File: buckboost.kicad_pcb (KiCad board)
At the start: 2 copper layers, 48.9 x 26 mm, 27 parts, among them K1 CONN_3, P1 CONN_2, P2 CONN_2, SW1 SPST, U1 TPS63060

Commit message: Revision 1
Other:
- board text added: "Revision 1"
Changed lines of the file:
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@@
     (area 64.694999 132.004999 113.740001 158.190001)
     (thickness 1.6)
-    (drawings 21)
+    (drawings 22)
     (tracks 104)
     (zones 0)
@@
     )
   )
+  (gr_text "Revision 1" (at 71.755 156.21) (layer B.SilkS)
+    (effects (font (size 1.5 1.5) (thickness 0.3)) (justify mirror))
+  )
   (gr_text "TPS63060 Power Supply\nby Amperture Engineering" (at 97.155 154.305) (layer B.SilkS)

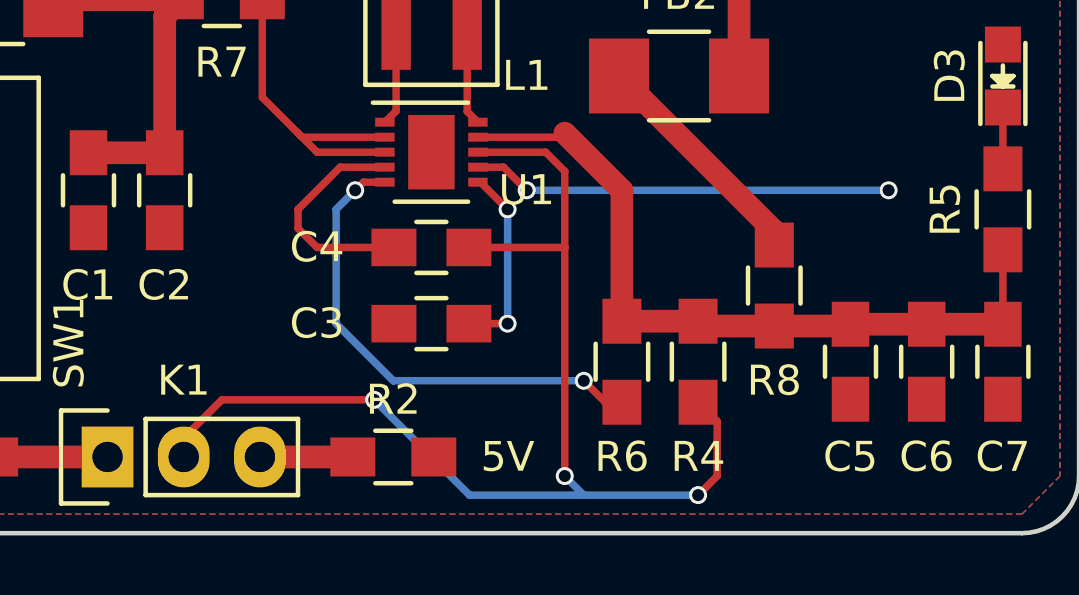
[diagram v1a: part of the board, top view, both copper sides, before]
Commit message: Fixing tracks for OSHPark design rules.
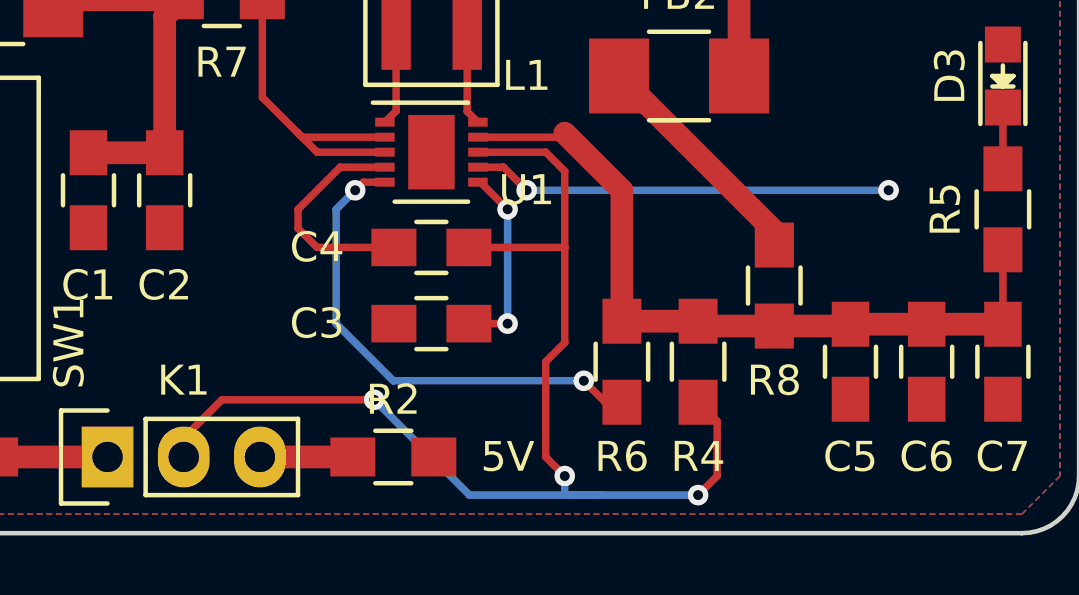
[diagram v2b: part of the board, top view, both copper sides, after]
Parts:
- gave numbers to parts that had none: 1
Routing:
- net FEEDBACK: track 40.7 -> 42.8 mm
- net PG: track 17.1 -> 17.6 mm
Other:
- net class Default: clearance 0.2 -> 0.1524; via_dia 0.6 -> 0.6858; via_drill 0.4 -> 0.3302
- rule trace_clearance: 0.2 -> 0.1524
- rule trace_min: 0.2 -> 0.1524
- rule via_min_drill: 0.3 -> 0.3302
- rule via_min_size: 0.4 -> 0.6858
- board text removed: "Revision 1"
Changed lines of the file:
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@@
     (area 64.694999 132.004999 113.740001 158.190001)
     (thickness 1.6)
-    (drawings 22)
-    (tracks 104)
+    (drawings 21)
+    (tracks 110)
     (zones 0)
     (modules 27)
@@
   (setup
     (last_trace_width 0.25)
-    (trace_clearance 0.2)
+    (trace_clearance 0.1524)
     (zone_clearance 0.508)
-    (zone_45_only no)
-    (trace_min 0.2)
+    (zone_45_only yes)
+    (trace_min 0.1524)
     (segment_width 0.2)
     (edge_width 0.15)
-    (via_size 0.6)
-    (via_drill 0.4)
-    (via_min_size 0.4)
-    (via_min_drill 0.3)
-    (uvia_size 0.3)
-    (uvia_drill 0.1)
+    (via_size 0.6858)
+    (via_drill 0.3302)
+    (via_min_size 0.6858)
+    (via_min_drill 0.3302)
+    (uvia_size 0.762)
+    (uvia_drill 0.508)
     (uvias_allowed no)
     (uvia_min_size 0)
@@
   (net 18 VOUT)
   (net_class Default "This is the default net class."
-    (clearance 0.2)
+    (clearance 0.1524)
     (trace_width 0.25)
-    (via_dia 0.6)
-    (via_drill 0.4)
-    (uvia_dia 0.3)
-    (uvia_drill 0.1)
+    (via_dia 0.6858)
+    (via_drill 0.3302)
+    (uvia_dia 0.762)
+    (uvia_drill 0.508)
     (add_net FEEDBACK)
     (add_net GND)
@@
     (descr "Symbol, OSHW-Logo, Silk Screen,")
     (tags "Symbol, OSHW-Logo, Silk Screen,")
-    (fp_text reference "" (at 0.09906 4.38912 180) (layer B.SilkS) hide
+    (fp_text reference REF** (at 0.09906 4.38912 180) (layer B.SilkS) hide
       (effects (font (size 1 1) (thickness 0.15)) (justify mirror))
     )
@@
     )
   )
-  (gr_text "Revision 1" (at 71.755 156.21) (layer B.SilkS)
-    (effects (font (size 1.5 1.5) (thickness 0.3)) (justify mirror))
-  )
   (gr_text "TPS63060 Power Supply\nby Amperture Engineering" (at 97.155 154.305) (layer B.SilkS)
     (effects (font (size 1.5 1.5) (thickness 0.3)) (justify mirror))
@@
   (segment (start 79.47 140.335) (end 83.9 135.905) (width 0.25) (layer F.Cu) (net 1))
   (segment (start 83.9 135.905) (end 83.9 135.255) (width 0.25) (layer F.Cu) (net 1))
+  (segment (start 93.625 145.915) (end 94.48 145.915) (width 0.25) (layer F.Cu) (net 2))
+  (via (at 107.315 146.685) (size 0.6858) (drill 0.3302) (layers F.Cu B.Cu) (net 2))
+  (segment (start 95.25 146.685) (end 107.315 146.685) (width 0.25) (layer B.Cu) (net 2))
+  (via (at 95.25 146.685) (size 0.6858) (drill 0.3302) (layers F.Cu B.Cu) (net 2))
+  (segment (start 94.48 145.915) (end 95.25 146.685) (width 0.25) (layer F.Cu) (net 2))
   (segment (start 90.525 145.915) (end 89.035 145.915) (width 0.25) (layer F.Cu) (net 2))
   (segment (start 88.265 148.59) (end 90.825 148.59) (width 0.25) (layer F.Cu) (net 2))
@@
   (segment (start 87.63 147.32) (end 87.63 147.955) (width 0.25) (layer F.Cu) (net 2))
   (segment (start 89.035 145.915) (end 87.63 147.32) (width 0.25) (layer F.Cu) (net 2))
-  (segment (start 93.625 145.915) (end 94.48 145.915) (width 0.25) (layer F.Cu) (net 2))
-  (via (at 107.315 146.685) (size 0.6) (drill 0.4) (layers F.Cu B.Cu) (net 2))
-  (segment (start 95.25 146.685) (end 107.315 146.685) (width 0.25) (layer B.Cu) (net 2))
-  (via (at 95.25 146.685) (size 0.6) (drill 0.4) (layers F.Cu B.Cu) (net 2))
-  (segment (start 94.48 145.915) (end 95.25 146.685) (width 0.25) (layer F.Cu) (net 2))
   (segment (start 93.625 146.415) (end 93.71 146.415) (width 0.25) (layer F.Cu) (net 3))
   (segment (start 93.71 146.415) (end 94.615 147.32) (width 0.25) (layer F.Cu) (net 3))
-  (via (at 94.615 147.32) (size 0.6) (drill 0.4) (layers F.Cu B.Cu) (net 3))
+  (segment (start 94.615 151.13) (end 93.325 151.13) (width 0.25) (layer F.Cu) (net 3))
+  (via (at 94.615 151.13) (size 0.6858) (drill 0.3302) (layers F.Cu B.Cu) (net 3))
   (segment (start 94.615 147.32) (end 94.615 151.13) (width 0.25) (layer B.Cu) (net 3))
-  (via (at 94.615 151.13) (size 0.6) (drill 0.4) (layers F.Cu B.Cu) (net 3))
-  (segment (start 94.615 151.13) (end 93.325 151.13) (width 0.25) (layer F.Cu) (net 3))
+  (via (at 94.615 147.32) (size 0.6858) (drill 0.3302) (layers F.Cu B.Cu) (net 3))
+  (segment (start 96.52 148.59) (end 96.52 151.765) (width 0.25) (layer F.Cu) (net 4))
+  (segment (start 96.52 156.845) (end 97.79 156.845) (width 0.25) (layer B.Cu) (net 4))
+  (segment (start 96.52 156.21) (end 96.52 156.845) (width 0.25) (layer B.Cu) (net 4))
+  (via (at 96.52 156.21) (size 0.6858) (drill 0.3302) (layers F.Cu B.Cu) (net 4))
+  (segment (start 95.885 155.575) (end 96.52 156.21) (width 0.25) (layer F.Cu) (net 4))
+  (segment (start 95.885 152.4) (end 95.885 155.575) (width 0.25) (layer F.Cu) (net 4))
+  (segment (start 96.52 151.765) (end 95.885 152.4) (width 0.25) (layer F.Cu) (net 4))
+  (segment (start 100.965 153.75) (end 101.6 154.385) (width 0.25) (layer F.Cu) (net 4))
+  (segment (start 101.6 154.385) (end 101.6 156.21) (width 0.25) (layer F.Cu) (net 4))
+  (segment (start 101.6 156.21) (end 100.965 156.845) (width 0.25) (layer F.Cu) (net 4))
+  (via (at 100.965 156.845) (size 0.6858) (drill 0.3302) (layers F.Cu B.Cu) (net 4))
+  (segment (start 100.965 156.845) (end 97.79 156.845) (width 0.25) (layer B.Cu) (net 4))
+  (segment (start 85.09 153.67) (end 83.82 154.94) (width 0.25) (layer F.Cu) (net 4))
+  (segment (start 97.79 156.845) (end 93.345 156.845) (width 0.25) (layer B.Cu) (net 4))
+  (segment (start 93.345 156.845) (end 90.17 153.67) (width 0.25) (layer B.Cu) (net 4))
+  (via (at 90.17 153.67) (size 0.6858) (drill 0.3302) (layers F.Cu B.Cu) (net 4))
+  (segment (start 90.17 153.67) (end 85.09 153.67) (width 0.25) (layer F.Cu) (net 4))
+  (segment (start 83.82 154.94) (end 83.82 155.575) (width 0.25) (layer F.Cu) (net 4))
   (segment (start 93.325 148.59) (end 96.52 148.59) (width 0.25) (layer F.Cu) (net 4))
   (segment (start 83.82 155.575) (end 83.82 154.94) (width 0.25) (layer F.Cu) (net 4))
-  (segment (start 83.82 154.94) (end 85.09 153.67) (width 0.25) (layer F.Cu) (net 4))
-  (segment (start 85.09 153.67) (end 90.17 153.67) (width 0.25) (layer F.Cu) (net 4))
-  (via (at 90.17 153.67) (size 0.6) (drill 0.4) (layers F.Cu B.Cu) (net 4))
-  (segment (start 90.17 153.67) (end 93.345 156.845) (width 0.25) (layer B.Cu) (net 4))
-  (segment (start 93.345 156.845) (end 97.155 156.845) (width 0.25) (layer B.Cu) (net 4))
   (segment (start 93.625 145.415) (end 95.885 145.415) (width 0.25) (layer F.Cu) (net 4))
-  (segment (start 101.6 156.21) (end 101.6 154.385) (width 0.25) (layer F.Cu) (net 4))
-  (segment (start 100.965 156.845) (end 101.6 156.21) (width 0.25) (layer F.Cu) (net 4))
-  (via (at 100.965 156.845) (size 0.6) (drill 0.4) (layers F.Cu B.Cu) (net 4))
-  (segment (start 97.155 156.845) (end 100.965 156.845) (width 0.25) (layer B.Cu) (net 4))
-  (segment (start 96.52 156.21) (end 97.155 156.845) (width 0.25) (layer B.Cu) (net 4))
-  (via (at 96.52 156.21) (size 0.6) (drill 0.4) (layers F.Cu B.Cu) (net 4))
   (segment (start 96.52 146.05) (end 96.52 148.59) (width 0.25) (layer F.Cu) (net 4))
-  (segment (start 96.52 148.59) (end 96.52 156.21) (width 0.25) (layer F.Cu) (net 4))
   (segment (start 95.885 145.415) (end 96.52 146.05) (width 0.25) (layer F.Cu) (net 4))
-  (segment (start 101.6 154.385) (end 100.965 153.75) (width 0.25) (layer F.Cu) (net 4))
   (segment (start 98.425 151.05) (end 98.425 146.685) (width 0.758) (layer F.Cu) (net 5))
   (segment (start 98.425 146.685) (end 96.52 144.78) (width 0.758) (layer F.Cu) (net 5))
@@
   (segment (start 90.525 146.415) (end 89.805 146.415) (width 0.25) (layer F.Cu) (net 12))
   (segment (start 97.155 153.035) (end 97.87 153.75) (width 0.25) (layer F.Cu) (net 12))
-  (via (at 97.155 153.035) (size 0.6) (drill 0.4) (layers F.Cu B.Cu) (net 12))
+  (via (at 97.155 153.035) (size 0.6858) (drill 0.3302) (layers F.Cu B.Cu) (net 12))
   (segment (start 90.805 153.035) (end 97.155 153.035) (width 0.25) (layer B.Cu) (net 12))
   (segment (start 88.9 151.13) (end 90.805 153.035) (width 0.25) (layer B.Cu) (net 12))
   (segment (start 88.9 147.32) (end 88.9 151.13) (width 0.25) (layer B.Cu) (net 12))
   (segment (start 89.535 146.685) (end 88.9 147.32) (width 0.25) (layer B.Cu) (net 12))
-  (via (at 89.535 146.685) (size 0.6) (drill 0.4) (layers F.Cu B.Cu) (net 12))
+  (via (at 89.535 146.685) (size 0.6858) (drill 0.3302) (layers F.Cu B.Cu) (net 12))
   (segment (start 89.805 146.415) (end 89.535 146.685) (width 0.25) (layer F.Cu) (net 12))
   (segment (start 97.87 153.75) (end 98.425 153.75) (width 0.25) (layer F.Cu) (net 12))
+  (segment (start 97.87 153.75) (end 98.425 153.75) (width 0.25) (layer F.Cu) (net 12))
   (segment (start 98.425 153.75) (end 98.425 154.305) (width 0.25) (layer F.Cu) (net 12))

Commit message: Housecleaning
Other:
- board text added: "Rev1"
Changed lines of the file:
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@@
     (area 64.694999 132.004999 113.740001 158.190001)
     (thickness 1.6)
-    (drawings 21)
+    (drawings 22)
     (tracks 110)
     (zones 0)
@@
   (page A4)
   (layers
-    (0 F.Cu signal)
-    (31 B.Cu signal)
-    (32 B.Adhes user)
-    (33 F.Adhes user)
-    (34 B.Paste user)
-    (35 F.Paste user)
+    (0 F.Cu signal hide)
+    (31 B.Cu signal hide)
+    (32 B.Adhes user hide)
+    (33 F.Adhes user hide)
+    (34 B.Paste user hide)
+    (35 F.Paste user hide)
     (36 B.SilkS user)
     (37 F.SilkS user)
-    (38 B.Mask user)
-    (39 F.Mask user)
-    (40 Dwgs.User user)
-    (41 Cmts.User user)
+    (38 B.Mask user hide)
+    (39 F.Mask user hide)
+    (40 Dwgs.User user hide)
+    (41 Cmts.User user hide)
     (42 Eco1.User user hide)
-    (43 Eco2.User user)
+    (43 Eco2.User user hide)
     (44 Edge.Cuts user)
     (45 Margin user)
@@
     (pad_to_mask_clearance 0.2)
     (aux_axis_origin 0 0)
-    (visible_elements FFFEFF7F)
+    (visible_elements FFFF3FFF)
     (pcbplotparams
-      (layerselection 0x00030_80000001)
-      (usegerberextensions false)
+      (layerselection 0x010f0_80000001)
+      (usegerberextensions true)
       (excludeedgelayer true)
       (linewidth 0.100000)
@@
       (outputformat 1)
       (mirror false)
-      (drillshape 1)
+      (drillshape 0)
       (scaleselection 1)
-      (outputdirectory ""))
+      (outputdirectory gerb/))
   )
   (net 0 "")
@@
     )
   )
-  (gr_text "TPS63060 Power Supply\nby Amperture Engineering" (at 97.155 154.305) (layer B.SilkS)
+  (gr_text Rev1 (at 109.855 155.575) (layer B.SilkS)
     (effects (font (size 1.5 1.5) (thickness 0.3)) (justify mirror))
   )
+  (gr_text "TPS63060 Power Supply\nby Amperture Engineering" (at 98.425 149.86) (layer B.SilkS)
+    (effects (font (size 1.5 1.5) (thickness 0.3)) (justify mirror))
+  )

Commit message: Preview of schematic
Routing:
- net Net-(C1-Pad1): track 28.4 -> 35.3 mm
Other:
- net class thick added: clearance 0.1524, trace_width 0.758, via_dia 0.6858, via_drill 0.3302
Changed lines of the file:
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@@
     (links 43)
     (no_connects 0)
-    (area 64.694999 132.004999 113.740001 158.190001)
+    (area 83.703572 83.43348 172.2224 156.775)
     (thickness 1.6)
     (drawings 22)
-    (tracks 110)
+    (tracks 112)
     (zones 0)
     (modules 27)
@@
   (page A4)
   (layers
-    (0 F.Cu signal hide)
-    (31 B.Cu signal hide)
-    (32 B.Adhes user hide)
-    (33 F.Adhes user hide)
-    (34 B.Paste user hide)
-    (35 F.Paste user hide)
+    (0 F.Cu signal)
+    (31 B.Cu signal)
+    (32 B.Adhes user)
+    (33 F.Adhes user)
+    (34 B.Paste user)
+    (35 F.Paste user)
     (36 B.SilkS user)
     (37 F.SilkS user)
-    (38 B.Mask user hide)
-    (39 F.Mask user hide)
+    (38 B.Mask user)
+    (39 F.Mask user)
     (40 Dwgs.User user hide)
     (41 Cmts.User user hide)
-    (42 Eco1.User user hide)
-    (43 Eco2.User user hide)
+    (42 Eco1.User user)
+    (43 Eco2.User user)
     (44 Edge.Cuts user)
     (45 Margin user)
@@
     (pad_to_mask_clearance 0.2)
     (aux_axis_origin 0 0)
-    (visible_elements FFFF3FFF)
+    (visible_elements FFFEFFBF)
     (pcbplotparams
       (layerselection 0x010f0_80000001)
@@
     (add_net FEEDBACK)
     (add_net GND)
-    (add_net "Net-(C1-Pad1)")
     (add_net "Net-(C3-Pad1)")
     (add_net "Net-(C5-Pad1)")
@@
     (add_net VOUT)
   )
+  (net_class thick ""
+    (clearance 0.1524)
+    (trace_width 0.758)
+    (via_dia 0.6858)
+    (via_drill 0.3302)
+    (uvia_dia 0.762)
+    (uvia_drill 0.508)
+    (add_net "Net-(C1-Pad1)")
+  )
   (module Symbols:Symbol_OSHW-Logo_SilkScreen (layer B.Cu)
     (at 69.85 135.89 180)
@@
       (effects (font (size 1 1) (thickness 0.15)) (justify mirror))
     )
-    (fp_text value Symbol_OSHW-Logo_SilkScreen (at 0.30988 -6.56082 180) (layer B.Fab)
+    (fp_text value Symbol_OSHW-Logo_SilkScreen (at 13.335 -24.765 180) (layer B.Fab) hide
       (effects (font (size 1 1) (thickness 0.15)) (justify mirror))
     )
@@
   (gr_line (start 113.665 132.08) (end 64.77 132.08) (angle 90) (layer Eco1.User) (width 0.2))
   (gr_line (start 113.665 132.715) (end 113.665 132.08) (angle 90) (layer Eco1.User) (width 0.2))
+  (segment (start 79.47 140.335) (end 79.47 139.685) (width 0.758) (layer F.Cu) (net 1))
+  (segment (start 79.47 139.685) (end 83.9 135.255) (width 0.758) (layer F.Cu) (net 1))
+  (segment (start 79.47 139.685) (end 83.9 135.255) (width 0.25) (layer F.Cu) (net 1))
   (segment (start 83.74 140.335) (end 83.74 135.415) (width 0.758) (layer F.Cu) (net 1))
   (segment (start 83.74 135.415) (end 83.9 135.255) (width 0.758) (layer F.Cu) (net 1))
@@
   (segment (start 83.185 140.89) (end 82.63 140.335) (width 0.25) (layer F.Cu) (net 1))
   (segment (start 82.63 140.335) (end 79.47 140.335) (width 0.25) (layer F.Cu) (net 1))
-  (segment (start 79.47 140.335) (end 83.9 135.905) (width 0.25) (layer F.Cu) (net 1))
   (segment (start 83.9 135.905) (end 83.9 135.255) (width 0.25) (layer F.Cu) (net 1))
   (segment (start 93.625 145.915) (end 94.48 145.915) (width 0.25) (layer F.Cu) (net 2))
